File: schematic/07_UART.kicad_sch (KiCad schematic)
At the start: 1 part, among them J9 UART0

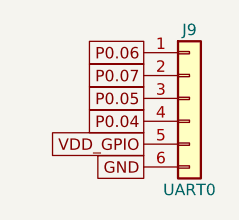
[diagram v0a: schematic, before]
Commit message: Pin remap + PCB sync (pass30cb): UART0 2-wire (RX P0.04, J9.2/3 NC), J16 DNF, U2 TLV73333 on PCB; ERC 0 errors; unconnected 43→38 (26 non-GND + 12 GND); short/clr/cross/hole 0
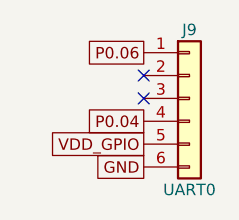
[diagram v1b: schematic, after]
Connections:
- net P0.05: no longer names the net of J9.3 (Pin_3)
- net P0.07: no longer names the net of J9.2 (Pin_2)
- no-connect marks 0 -> 2
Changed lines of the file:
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@@
-		)
-	)
-	(global_label "P0.07"
-		(at 71.12 60.96 180)
-		(effects
-			(font
-				(size 1.27 1.27)
-			)
-			(justify right)
-		)
-	)
-	(global_label "P0.05"
-		(at 71.12 63.5 180)
-		(effects
-			(font
-				(size 1.27 1.27)
-			)
-			(justify right)
 		)
 	)
@@
 		)
 	)
+	(no_connect
+		(at 71.12 60.96)
+	)
+	(no_connect
+		(at 71.12 63.5)
+	)
 	(sheet_instances

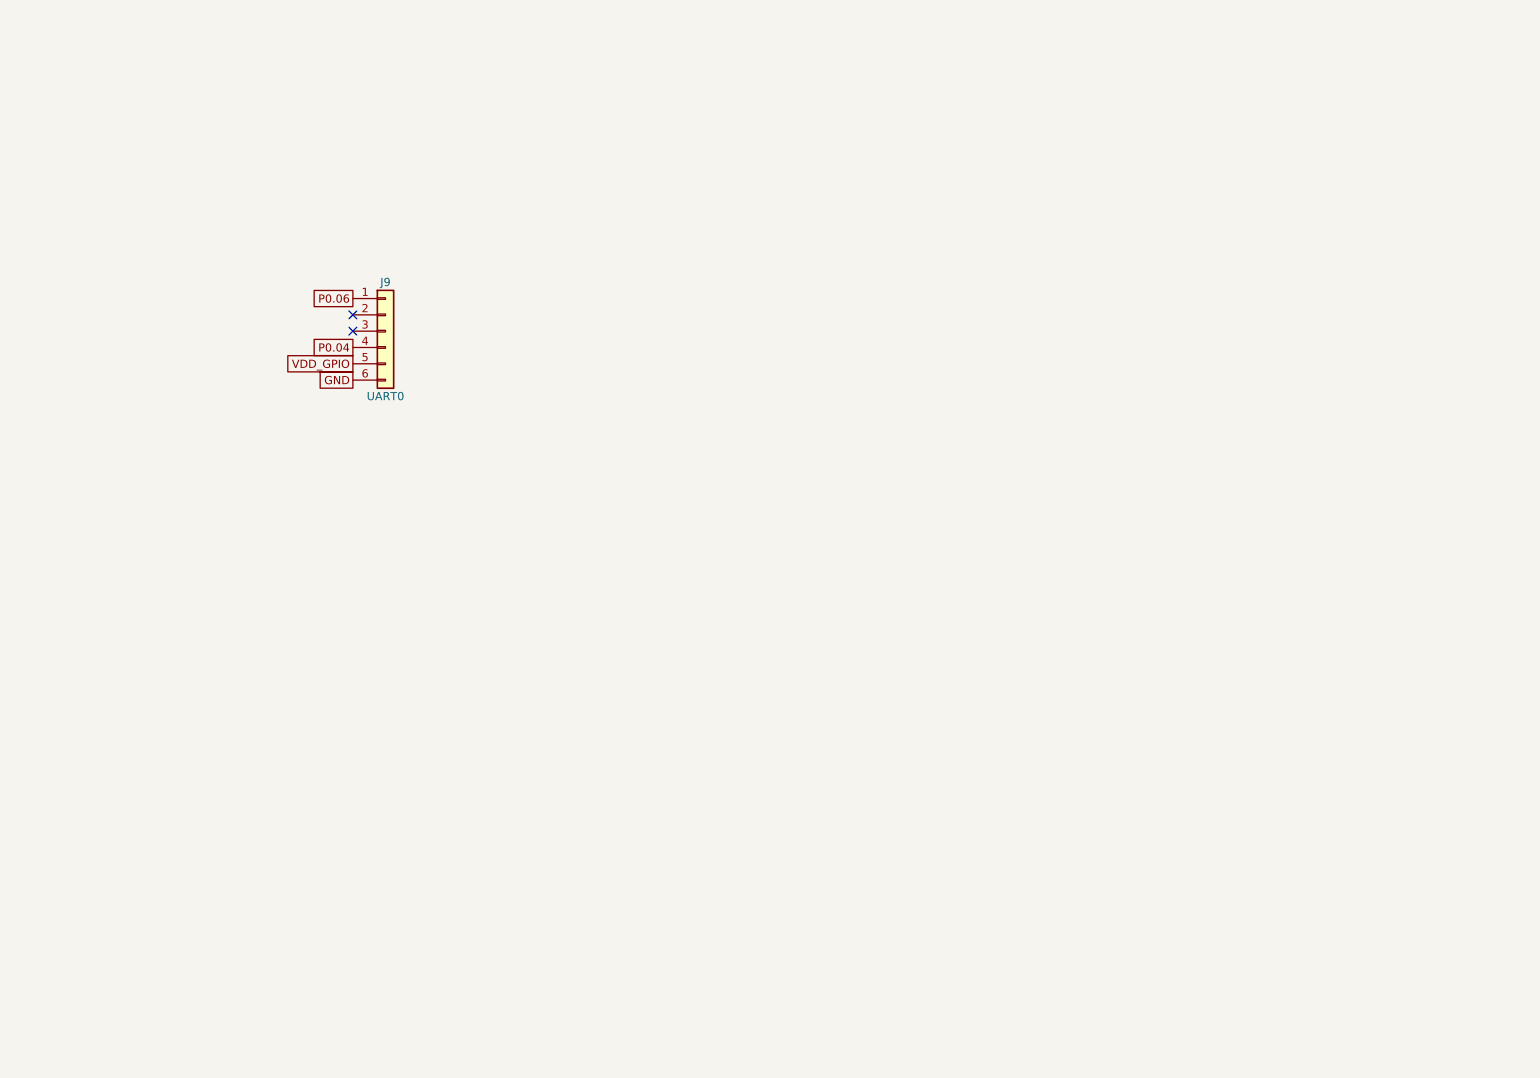
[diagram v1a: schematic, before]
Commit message: v2: simplify to UART modem module (J20 host header, LXC translators); remove J1, J3, J6, J9-J18, optional parts
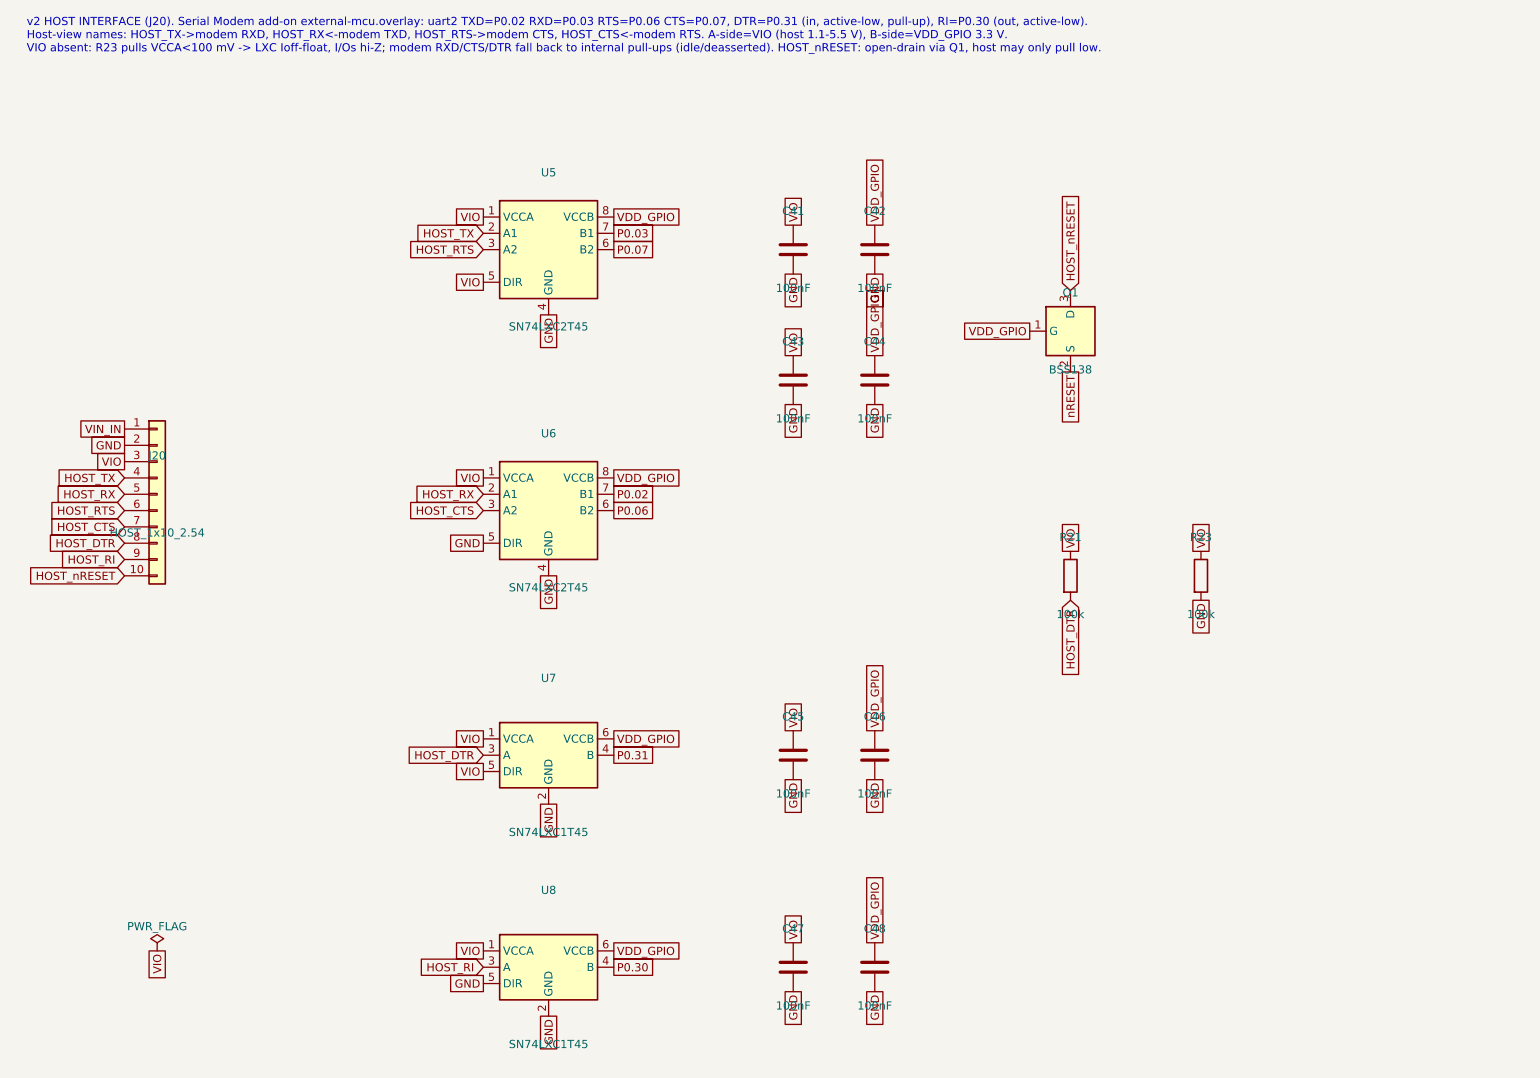
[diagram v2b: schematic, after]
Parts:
- removed J9: UART0, Connector_PinHeader_2.54mm:PinHeader_1x06_P2.54mm_Vertical, symbol Connector_Generic:Conn_01x06
- added C41, C42, C43, C44, C45, C46, C47, C48: 100nF, Capacitor_SMD:C_0402_1005Metric, symbol Device:C
- added J20: HOST_1x10_2.54, Connector_PinHeader_2.54mm:PinHeader_1x10_P2.54mm_Vertical, symbol Connector_Generic:Conn_01x10
- added Q1: BSS138, Package_TO_SOT_SMD:SOT-23, symbol nRF9161_v2:BSS138
- added R21, R23: 100k, Resistor_SMD:R_0402_1005Metric, symbol Device:R
- added U5, U6: SN74LXC2T45, Package_SO:VSSOP-8_2.3x2mm_P0.5mm, symbol nRF9161_v2:SN74LXC2T45DCU
- added U7, U8: SN74LXC1T45, Package_TO_SOT_SMD:SOT-23-6, symbol nRF9161_v2:SN74LXC1T45DBV
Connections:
- net GND: now also C41.2, C42.2, C43.2, C44.2, C45.2, C46.2, C47.2, C48.2, J20.2 (Pin_2), R23.2, U5.4 (GND), U6.4 (GND), U6.5 (DIR), U7.2 (GND), U8.2 (GND), U8.5 (DIR)
- net P0.06: now also U6.6 (B2)
- net VDD_GPIO: now also C42.1, C44.1, C46.1, C48.1, Q1.1 (G), U5.8 (VCCB), U6.8 (VCCB), U7.6 (VCCB), U8.6 (VCCB)
- new net HOST_CTS: J20.7 (Pin_7), U6.3 (A2)
- new net HOST_DTR: J20.8 (Pin_8), R21.2, U7.3 (A)
- new net HOST_RI: J20.9 (Pin_9), U8.3 (A)
- new net HOST_RTS: J20.6 (Pin_6), U5.3 (A2)
- new net HOST_RX: J20.5 (Pin_5), U6.2 (A1)
- new net HOST_TX: J20.4 (Pin_4), U5.2 (A1)
- new net HOST_nRESET: J20.10 (Pin_10), Q1.3 (D)
- new net P0.02: U6.7 (B1)
- new net P0.03: U5.7 (B1)
- new net P0.07: U5.6 (B2)
- new net P0.30: U8.4 (B)
- new net P0.31: U7.4 (B)
- new net VIN_IN: J20.1 (Pin_1)
- new net VIO: C41.1, C43.1, C45.1, C47.1, J20.3 (Pin_3), R21.1, R23.1, U5.1 (VCCA), U5.5 (DIR), U6.1 (VCCA), U7.1 (VCCA), U7.5 (DIR), U8.1 (VCCA)
- new net nRESET: Q1.2 (S)
- no-connect marks 2 -> 0
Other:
- note added: "v2 HOST INTERFACE (J20). Serial Modem add-on external-mcu.overlay: uart2 TXD=P0.02 RXD=P0.03 RTS=P0.06 CTS=P0.07, DTR=P0.31 (in, active-low, pull-up), RI=P0.30 (out, active-low). Host-view names: HOST_TX->modem RXD, HOST_RX<-modem TXD, HOST_RTS->modem CTS, HOST_CTS<-modem RTS. A-side=VIO (host 1.1-5.5 V), B-side=VDD_GPIO 3.3 V. VIO absent: R23 pulls VCCA<100 mV -> LXC Ioff-float, I/Os hi-Z; modem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"

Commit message: v2 BOM: apply footprint-consistent MPNs + LCSC IDs, JLC BOM, audit reports (U4 footprint pending Layout)
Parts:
- J20: MPN 2.54-1*10PPin -> 2.54-1*10P
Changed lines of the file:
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@@
 			)
 		)
-		(property "MPN" "2.54-1*10PPin"
+		(property "MPN" "2.54-1*10P"
 			(at 40.64 88.9 0)
 			(hide yes)
